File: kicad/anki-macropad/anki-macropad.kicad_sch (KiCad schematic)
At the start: 27 parts, among them J1 USB_C_Receptacle_USB2.0_14P, J2 Conn_01x02, U1 RP2040, U2 NCP1117-3.3_SOT223, U3 W25Q128JVS, U4 USBLC6-2SC6, X1 ABM8-272-T3

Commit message: Working on schematic
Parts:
- added C2, C3: 15p, symbol Device:C
- added D1, D2, D3, D4, D5, D6: Diode, symbol Device:D
- added MX1, MX2, MX3, MX4, MX5, MX6: MX_SW_solder, PCM_marbastlib-mx:SW_MX_1u, symbol PCM_marbastlib-mx:MX_SW_solder
- added R5: 1k, symbol Device:R
- X1: footprint ABM8-272-T3_ABR -> ABM8_272_T3:ABM8-272-T3_ABR
- renumbered R5 to R6, R6 to R7
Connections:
- net GND: now also X1.2, X1.4, C2.1, C3.1
- net XIN: now also X1.1, C2.2
- net XOUT: now also R5.2
- net at X1.3: now also C3.2, R5.1
- new net: D2.2 (A), MX2.2
- new net: D5.2 (A), MX5.2
- new net: D4.2 (A), MX4.2
- new net: D3.2 (A), MX3.2
- new net: D6.2 (A), MX6.2
- new net: D1.2 (A), MX1.2
- new net COLUMN 0: MX1.1
- new net COLUMN 1: MX2.1
- new net COLUMN 2: MX3.1
- new net COLUMN 3: MX4.1, MX5.1, MX6.1
- new net ROW 0: D1.1 (K), D2.1 (K), D3.1 (K), D4.1 (K)
- new net ROW 1: D5.1 (K)
- new net ROW 2: D6.1 (K)
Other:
- note added: "KEY MATRIX"
- title: (none) -> RP2040 Anki Macropad
- moved on the sheet: C1, C10, C11, C12, C13, C14, C15, C16, C4, C5, C6, C7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

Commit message: Working on schematic
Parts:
- removed J2: Conn_01x02, symbol Connector_Generic:Conn_01x02
- added SW1, SW2: SW_Push, symbol Switch:SW_Push
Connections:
- net GPIO0 is gone; now on net ROW 0: U1.2 (GPIO0)
- net GPIO1 is gone; now on net ROW 1: U1.3 (GPIO1)
- net GPIO2 is gone; now on net ROW 2: U1.4 (GPIO2)
- net GPIO4 is gone; now on net COLUMN 0: U1.6 (GPIO4)
- net GPIO5 is gone; now on net COLUMN 1: U1.7 (GPIO5)
- net GPIO6 is gone; now on net COLUMN 2: U1.8 (GPIO6)
- net GPIO7 is gone; now on net COLUMN 3: U1.9 (GPIO7)
- net GND: now also SW1.2
- net GPIO10: no longer names the net of U1.13 (GPIO10)
- net GPIO11: no longer names the net of U1.14 (GPIO11)
- net GPIO12: no longer names the net of U1.15 (GPIO12)
- net GPIO13: no longer names the net of U1.16 (GPIO13)
- net GPIO14: no longer names the net of U1.17 (GPIO14)
- net GPIO15: no longer names the net of U1.18 (GPIO15)
- net GPIO16: no longer names the net of U1.27 (GPIO16)
- net GPIO17: no longer names the net of U1.28 (GPIO17)
- net GPIO18: no longer names the net of U1.29 (GPIO18)
- net GPIO19: no longer names the net of U1.30 (GPIO19)
- net GPIO20: no longer names the net of U1.31 (GPIO20)
- net GPIO21: no longer names the net of U1.32 (GPIO21)
- net GPIO22: no longer names the net of U1.34 (GPIO22)
- net GPIO23: no longer names the net of U1.35 (GPIO23)
- net GPIO24: no longer names the net of U1.36 (GPIO24)
- net GPIO25: no longer names the net of U1.37 (GPIO25)
- net GPIO26_ADC0: no longer names the net of U1.38 (GPIO26_ADC0)
- net GPIO27_ADC1: no longer names the net of U1.39 (GPIO27_ADC1)
- net GPIO28_ADC2: no longer names the net of U1.40 (GPIO28_ADC2)
- net GPIO29_ADC3: no longer names the net of U1.41 (GPIO29_ADC3)
- net GPIO3: no longer names the net of U1.5 (GPIO3)
- net GPIO8: no longer names the net of U1.11 (GPIO8)
- net GPIO9: no longer names the net of U1.12 (GPIO9)
- net SWCLK: no longer names the net of U1.24 (SWCLK)
- net SWD: no longer names the net of U1.25 (SWD)
- net ~{USB_BOOT} renamed USB_BOOT
- net USB_BOOT: now also SW1.1
- no-connect marks 0 -> 26

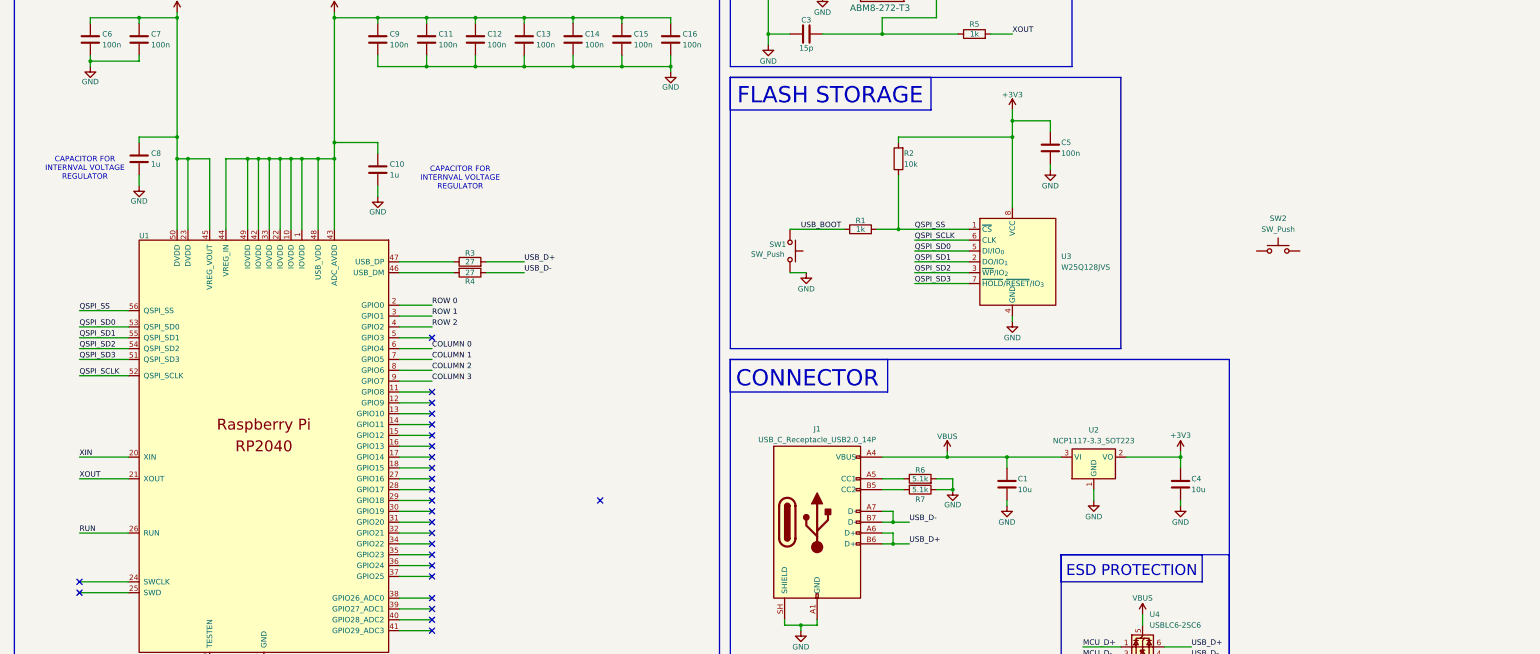
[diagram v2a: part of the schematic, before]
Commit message: Finished schematic, started pcb
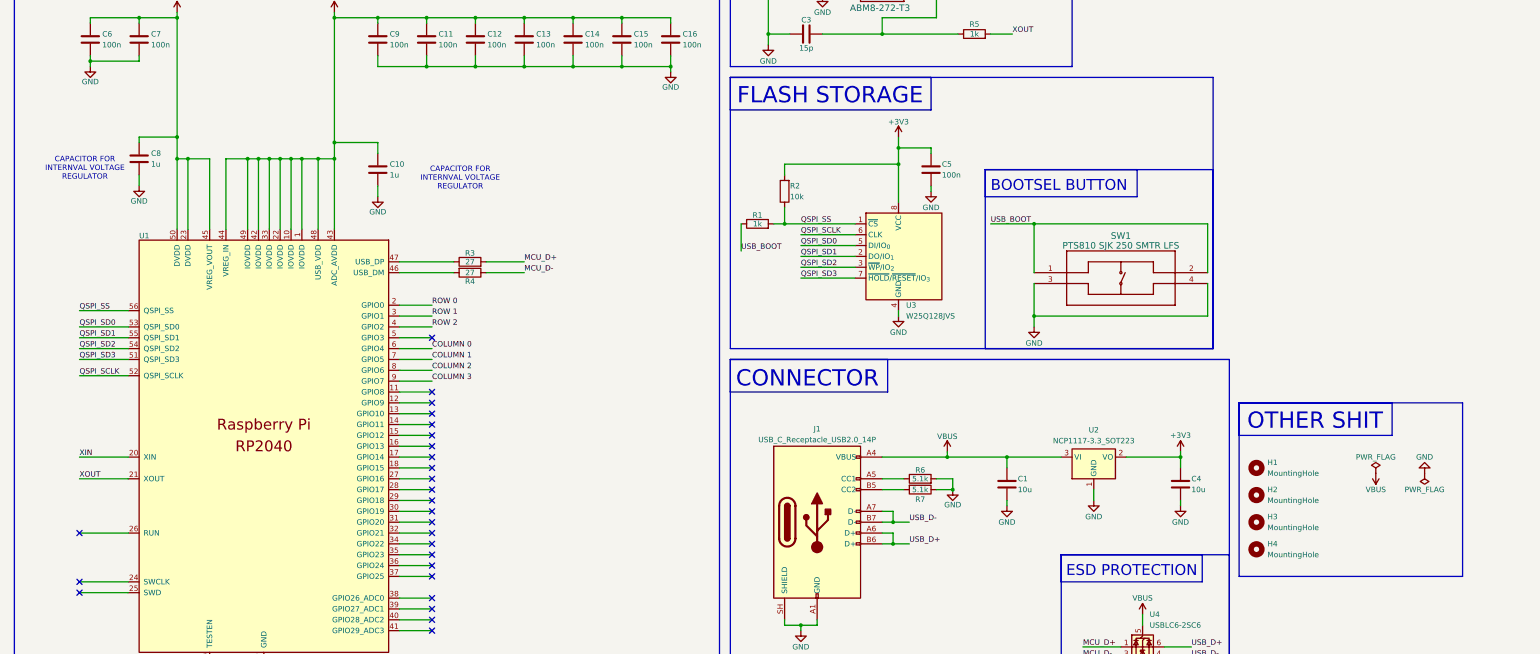
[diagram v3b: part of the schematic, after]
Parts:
- removed SW1, SW2: SW_Push, symbol Switch:SW_Push
- added H1, H2, H3, H4: MountingHole, MountingHole:MountingHole_2.7mm_M2.5, symbol Mechanical:MountingHole
- added SW1: PTS810 SJK 250 SMTR LFS, PTS810_CNK:PTS810_CNK, symbol PTS810_CNK:PTS810_SJK_250_SMTR_LFS
- C1, C4: footprint (none) -> Capacitor_SMD:C_0805_2012Metric
- C10, C11, C12, C13, C14, C15, C16, C2, C3, C5, C6, C7, C8, C9: footprint (none) -> Capacitor_SMD:C_0402_1005Metric
- D1, D2, D3, D4, D5, D6: footprint (none) -> Diode_SMD:D_SOD-123
- J1: footprint (none) -> USB_C_HRO_TYPE-C-31-M-12:USB_C_HRO_TYPE-C-31-M-12
- R1, R2, R3, R4, R5, R6, R7: footprint (none) -> Resistor_SMD:R_0402_1005Metric
- U1: footprint RP2040_minimal:RP2040-QFN-56 -> RP2040-QFN-56:RP2040-QFN-56
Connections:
- net GND: now also SW1.3, SW1.4
- net MCU_D+: now also R3.2
- net MCU_D-: now also R4.1
- net USB_BOOT: now also SW1.1, SW1.2
- net USB_D+: no longer R3.2
- net USB_D-: no longer R4.1
- net RUN: no longer names the net of U1.26 (RUN)
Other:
- note added: "BOOTSEL BUTTON"
- note added: "OTHER SHIT"
- moved on the sheet: C5, R1, R2, U3

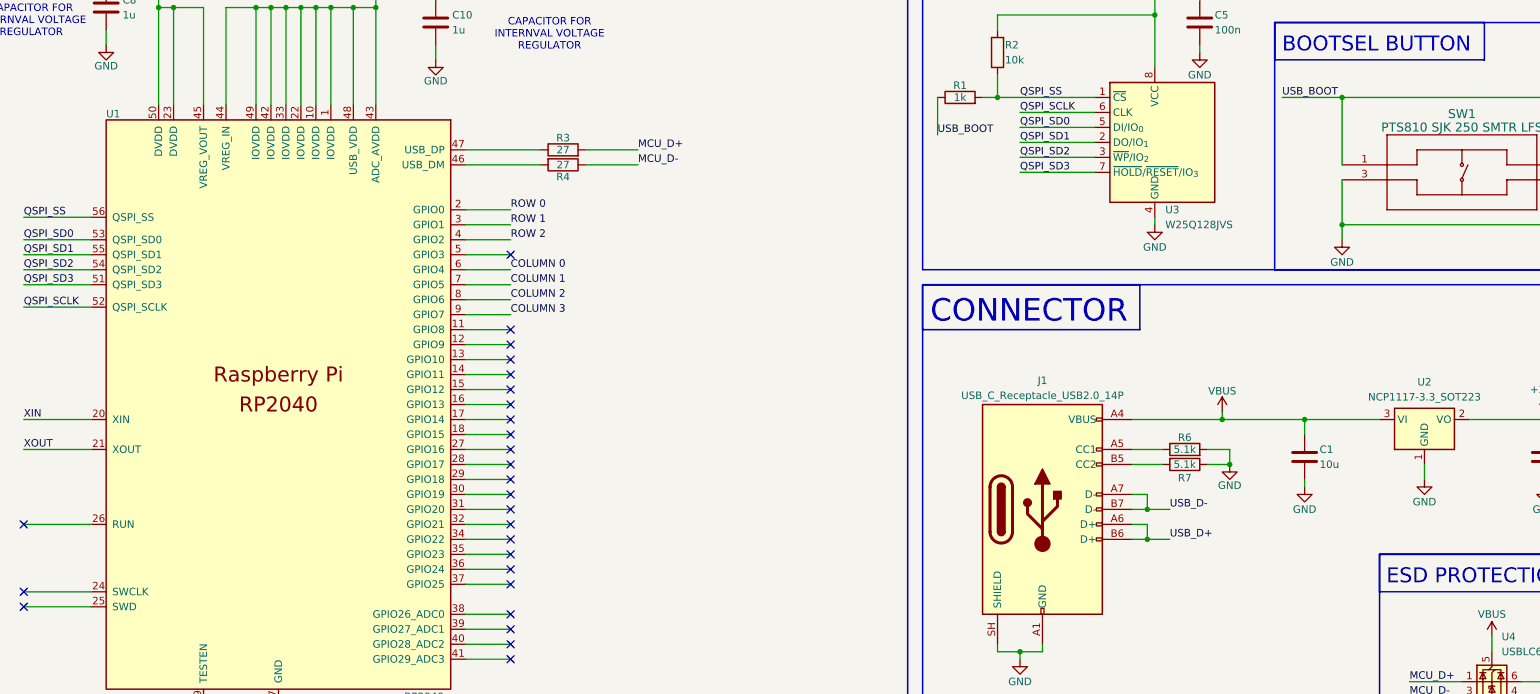
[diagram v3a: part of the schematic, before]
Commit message: Worked on PCB layout and traces
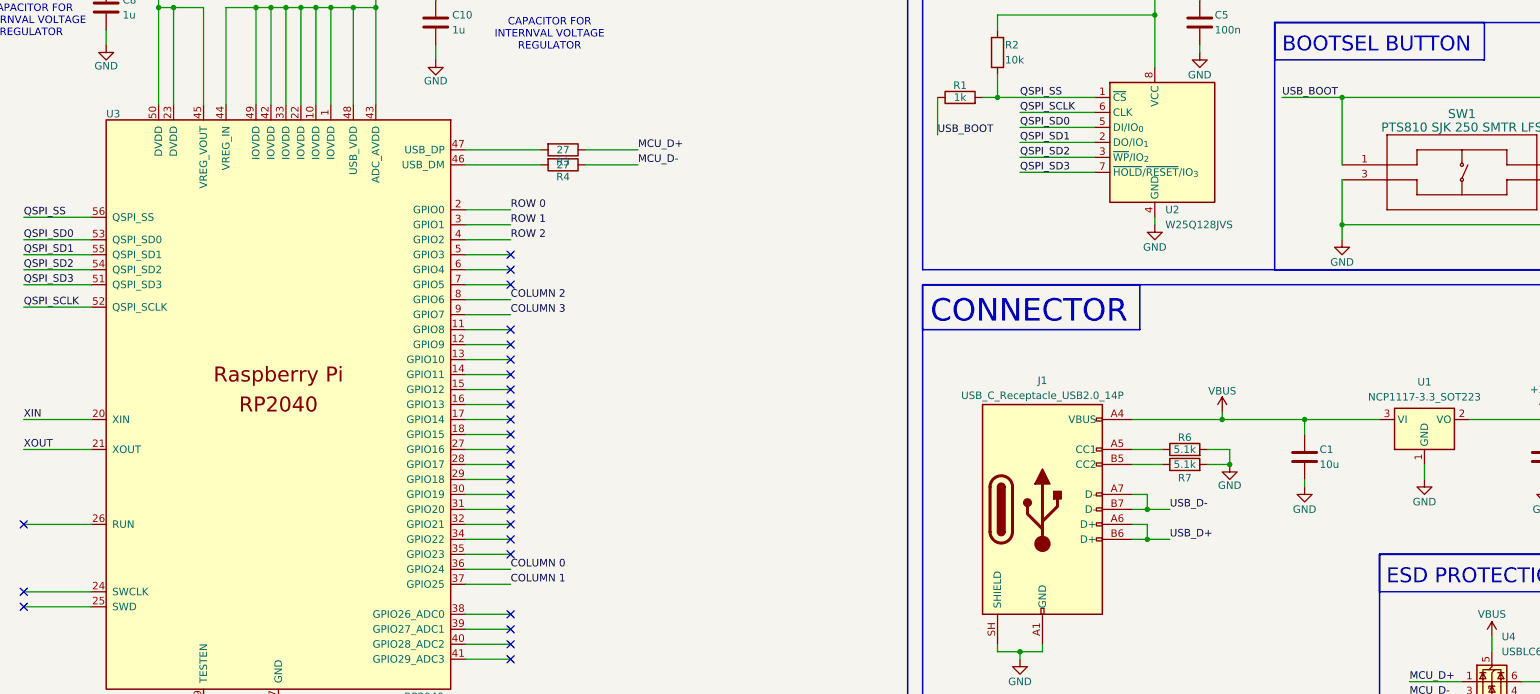
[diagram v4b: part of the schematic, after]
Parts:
- renumbered U2 to U1, U3 to U2, U1 to U3
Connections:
- net COLUMN 0: now also U3.36 (GPIO24); no longer U3.6 (GPIO4)
- net COLUMN 1: now also U3.37 (GPIO25); no longer U3.7 (GPIO5)
- net GND: now also R7.2; no longer R7.1
- net MCU_D+: now also R3.1; no longer R3.2
- net at J1.B5 (CC2): now also R7.1; no longer R7.2
- net at U3.47 (USB_DP): now also R3.2; no longer R3.1
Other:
- moved on the sheet: R3, R7
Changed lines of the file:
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@@
 	)
 	(no_connect
+		(at 111.76 196.85)
+	)
+	(no_connect
 		(at 111.76 227.33)
 	)
@@
 	)
 	(no_connect
-		(at 111.76 250.19)
-	)
-	(no_connect
 		(at 111.76 217.17)
 	)
@@
 	)
 	(no_connect
+		(at 111.76 199.39)
+	)
+	(no_connect
 		(at 111.76 207.01)
 	)
@@
 	)
 	(no_connect
-		(at 111.76 247.65)
-	)
-	(no_connect
 		(at 111.76 242.57)
 	)
@@
 		)
 	)
-	(label "COLUMN 1"
-		(at 111.76 199.39 0)
-		(effects
-			(font
-				(size 1.27 1.27)
-			)
-			(justify left bottom)
-		)
-	)
 	(label "QSPI_SD1"
 		(at 29.21 194.31 0)
@@
 		)
 	)
-	(label "COLUMN 0"
-		(at 111.76 196.85 0)
-		(effects
-			(font
-				(size 1.27 1.27)
-			)
-			(justify left bottom)
-		)
-	)
 	(label "COLUMN 3"
 		(at 374.65 40.64 90)
@@
 		)
 	)
+	(label "COLUMN 1"
+		(at 111.76 250.19 0)
+		(effects
+			(font
+				(size 1.27 1.27)
+			)
+			(justify left bottom)
+		)
+	)
 	(label "USB_D-"
 		(at 289.56 269.24 0)
@@
 		)
 	)
+	(label "COLUMN 0"
+		(at 111.76 247.65 0)
+		(effects
+			(font
+				(size 1.27 1.27)
+			)
+			(justify left bottom)
+		)
+	)
 	(label "QSPI_SD0"
 		(at 29.21 191.77 0)
@@
 	(symbol
 		(lib_id "Device:R")
-		(at 120.65 176.53 90)
+		(at 120.65 176.53 270)
 		(unit 1)
 		(body_style 1)
@@
 		(dnp no)
 		(property "Reference" "R3"
-			(at 120.65 174.498 90)
+			(at 120.65 178.562 90)
 			(show_name no)
 			(do_not_autoplace no)
@@
 		)
 		(property "Footprint" "Resistor_SMD:R_0402_1005Metric"
-			(at 120.65 178.308 90)
+			(at 120.65 174.752 90)
 			(hide yes)
 			(show_name no)
@@
 		(dnp no)
 		(fields_autoplaced yes)
-		(property "Reference" "U2"
+		(property "Reference" "U1"
 			(at 266.7 215.9 0)
 			(show_name no)
@@
 			(project "anki-macropad"
 				(path "/601e356b-8d57-4612-aef2-e702ce6eb0da"
-					(reference "U2")
+					(reference "U1")
 					(unit 1)
 				)
@@
 		(in_pos_files yes)
 		(dnp no)
-		(property "Reference" "U1"
+		(property "Reference" "U3"
 			(at 43.18 170.434 0)
 			(show_name no)
@@
 			(project "anki-macropad"
 				(path "/601e356b-8d57-4612-aef2-e702ce6eb0da"
-					(reference "U1")
+					(reference "U3")
 					(unit 1)
 				)
@@
 		(in_pos_files yes)
 		(dnp no)
-		(property "Reference" "U3"
+		(property "Reference" "U2"
 			(at 222.758 186.69 0)
 			(show_name no)
@@
 			(project "anki-macropad"
 				(path "/601e356b-8d57-4612-aef2-e702ce6eb0da"
-					(reference "U3")
+					(reference "U2")
 					(unit 1)
 				)
@@
 	(symbol
 		(lib_id "Device:R")
-		(at 226.06 229.87 270)
+		(at 226.06 229.87 90)
 		(unit 1)
 		(body_style 1)
@@
 		)
 		(property "Footprint" "Resistor_SMD:R_0402_1005Metric"
-			(at 226.06 228.092 90)
+			(at 226.06 231.648 90)
 			(hide yes)
 			(show_name no)

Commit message: Pretty much finished the PCB. Just need to go through DRC.
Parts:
- removed H1, H2, H3, H4: MountingHole, MountingHole:MountingHole_2.7mm_M2.5, symbol Mechanical:MountingHole
- added H1, H2, H3, H4: MountingHole_Pad, MountingHole:MountingHole_2.7mm_M2.5_Pad, symbol Mechanical:MountingHole_Pad
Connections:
- net GND: now also H1.1, H2.1, H3.1, H4.1
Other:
- note added: "OTHER STUFF"
- note removed: "OTHER SHIT"
